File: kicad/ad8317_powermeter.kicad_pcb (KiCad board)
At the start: 2 copper layers, 18.2 x 13.5 mm, 37 parts, among them J1 Conn_Coaxial, U1 AD8317, U2 STM32F373RCTx, U3 REF3030, U4 ADP150AUJZ-3.3-R7

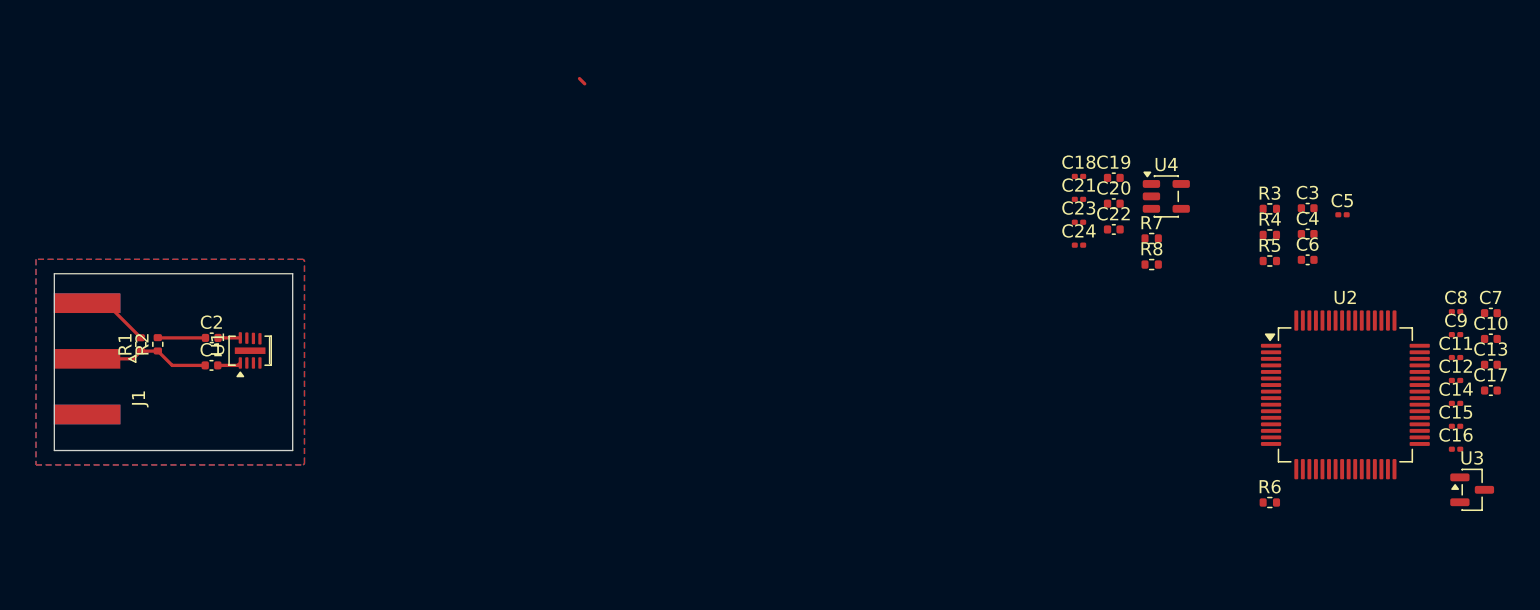
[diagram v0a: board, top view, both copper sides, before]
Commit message: Add calibration scripts, documentation, simulation tools, and KiCad updates
- cal/calibration.py: 3-phase RF linearity calibration (29 freq, 28 power steps,
  1 MHz–10 GHz, direct generator→DUT, no attenuator, NRP sensor 0.01 dBm precision)
- cal/temp_calibration.py: temperature calibration via Vötsch chamber (16–40°C,
  Vötsch SIMSERV TCP driver, tracking generator source, outputs TEMP_COEFF_DB_PER_C[])
- cal/results/: dry-run calibration tables (.h/.json), figures, PDF reports
- doc/: ADC signal path analysis, calibration procedure (3-phase), lab optimisation
  guide updated for 1 MHz–10 GHz range and temperature correction firmware formula
- doc/diagrams/: PlantUML/Mermaid source + rendered PNGs for pipeline, firmware,
  and RF signal chain architectures
- sim/ltpwr_to_touchstone.py: LTpowerAnalyzer Z(f) → Touchstone S1P + Z1P via
  scikit-rf for SIwave PI-AC Decoupling Optimization DC/DC source impedance import
- sim/Measured_source_impedance.txt/.s1p/.z1p: DC/DC output impedance measurement
  and converted Touchstone files (100 Hz–10 MHz, 201 points)
- kicad/: updated schematics (MCU, power management, RF frontend, UI) and PCB layout
- kicad/fixture-rev_A/: test fixture DXF drawings
- lib/: Würth 744231091 datasheet, Hammond 1590A board outline footprint
- pp_3d_printer_setup_spec.md, pp_horn_antenna_manufacturing_spec.md: process specs

Co-Authored-By: Claude Sonnet 4.6 <noreply@anthropic.com>
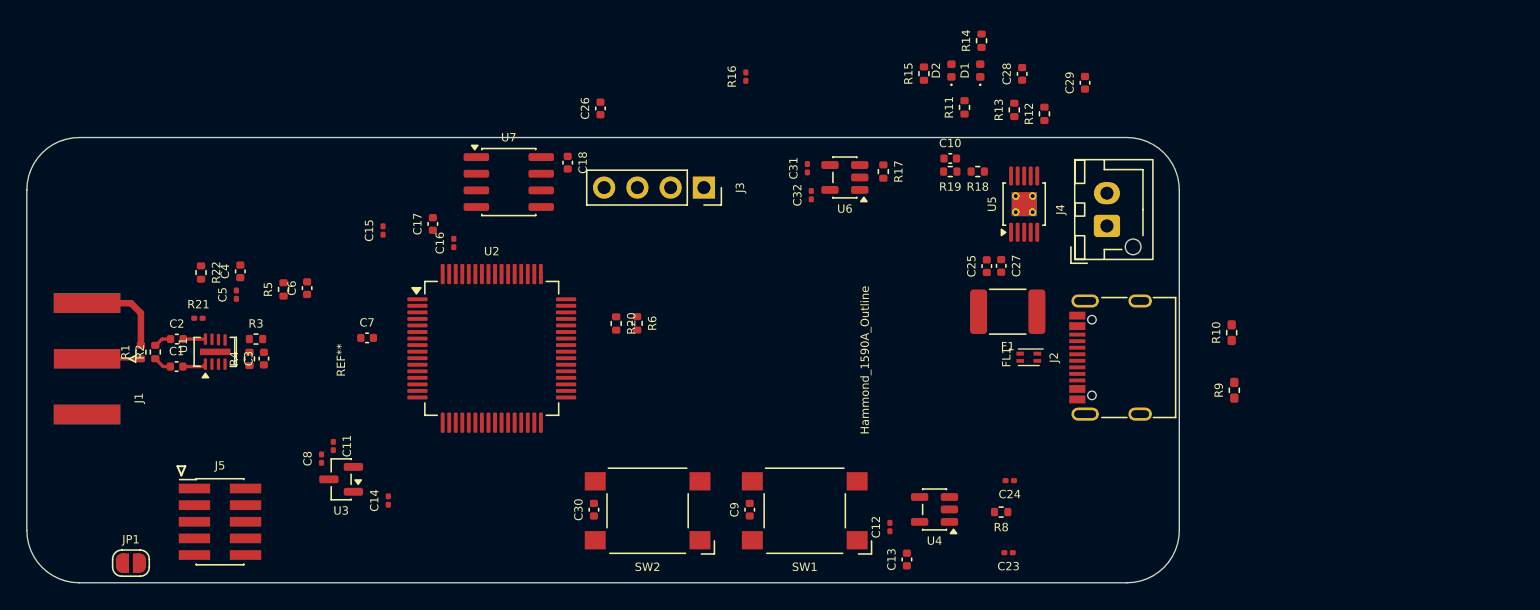
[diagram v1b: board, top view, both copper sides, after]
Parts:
- removed C19, C20: 100nF, Capacitor_SMD:C_0402_1005Metric
- removed C21: 10uF/, Capacitor_SMD:C_0201_0603Metric
- removed C22: 47nF, Capacitor_SMD:C_0402_1005Metric
- removed R7: 100R, Resistor_SMD:R_0402_1005Metric
- added C25: 100nF, Capacitor_SMD:C_0402_1005Metric, F.Cu at (206.4, 77.9)
- added C26: 100nF, Capacitor_SMD:C_0402_1005Metric, F.Cu at (176.9, 65.9)
- added C27: 100nF, Capacitor_SMD:C_0402_1005Metric, F.Cu at (207.5, 77.9)
- added C28: 10uF/16V, Capacitor_SMD:C_0402_1005Metric, F.Cu at (209.1, 63.2)
- added C29: 10uF/16V, Capacitor_SMD:C_0402_1005Metric, F.Cu at (213.9, 63.9)
- added C30: 100nF, Capacitor_SMD:C_0402_1005Metric, F.Cu at (176.4, 96.5)
- added C31: 1uF/, Capacitor_SMD:C_0201_0603Metric, F.Cu at (192.7, 70.4)
- added C32: 1uF/, Capacitor_SMD:C_0201_0603Metric, F.Cu at (193.0, 72.5)
- added D1: LED, LED_SMD:LED_0402_1005Metric, F.Cu at (205.9, 63.0)
- added D2: LED, LED_SMD:LED_0402_1005Metric, F.Cu at (203.7, 63.0)
- added F1: 2A max / 8V max, Fuse:Fuse_1812_4532Metric_Pad1.30x3.40mm_HandSolder, F.Cu at (208.0, 81.4)
- added FL1: 0603USB-142, Inductor_SMD:L_CommonModeChoke_Coilcraft_0603USB, F.Cu at (209.6, 84.9)
- added J2: USB_C_Receptacle_USB2.0_16P, Connector_USB:USB_C_Receptacle_G-Switch_GT-USB-7010ASV, F.Cu at (217.0, 84.9)
- added J3: Conn_01x04_Pin, Connector_PinSocket_2.54mm:PinSocket_1x04_P2.54mm_Vertical, F.Cu at (184.8, 71.9)
- added J4: Conn_01x02_Pin, Connector_JST:JST_XH_B2B-XH-AM_1x02_P2.50mm_Vertical, F.Cu at (215.6, 74.8)
- added J5: Conn_ARM_JTAG_SWD_10_UART, Connector_PinHeader_1.27mm:PinHeader_2x05_P1.27mm_Vertical_SMD, F.Cu at (147.8, 97.4)
- added JP1: Small_Open, Jumper:SolderJumper-2_P1.3mm_Open_RoundedPad1.0x1.5mm, F.Cu at (141.1, 100.6)
- added R10: 5K1, Resistor_SMD:R_0402_1005Metric_Pad0.72x0.64mm_HandSolder, F.Cu at (225.1, 83.0)
- added R11: 1k, Resistor_SMD:R_0402_1005Metric, F.Cu at (204.7, 65.8)
- added R12: 2k, Resistor_SMD:R_0402_1005Metric, F.Cu at (210.8, 66.3)
- added R13: 0R, Resistor_SMD:R_0402_1005Metric, F.Cu at (208.5, 66.0)
- added R14: 1k5, Resistor_SMD:R_0402_1005Metric, F.Cu at (206.0, 60.7)
- added R15: 1k5, Resistor_SMD:R_0402_1005Metric, F.Cu at (201.6, 63.2)
- added R16: 10k NTC Thermistor, Capacitor_SMD:C_0201_0603Metric, F.Cu at (188.0, 63.5)
- added R17: 100k, Resistor_SMD:R_0402_1005Metric, F.Cu at (198.5, 70.7)
- added R18: 100k, Resistor_SMD:R_0402_1005Metric, F.Cu at (205.7, 70.7)
- added R19: 100k, Resistor_SMD:R_0402_1005Metric, F.Cu at (203.6, 70.7)
- added R20: 10K, Resistor_SMD:R_0402_1005Metric, F.Cu at (178.1, 82.3)
- added R21: 10k NTC Thermistor, Capacitor_SMD:C_0201_0603Metric, F.Cu at (146.2, 81.9)
- added R22: 100k, Resistor_SMD:R_0402_1005Metric, F.Cu at (146.4, 78.4)
- added R9: 5K1, Resistor_SMD:R_0402_1005Metric_Pad0.72x0.64mm_HandSolder, F.Cu at (225.3, 87.4)
- added REF**: Hammond_1590A_Outline, ad8317_custom:Hammond_1590A_Board_Outline, F.Cu at (177.1, 85.1)
- added SW1: SW_Omron_B3FS, Button_Switch_SMD:SW_SPST_Omron_B3FS-100xP, F.Cu at (192.5, 96.6)
- added SW2: SW_Omron_B3FS, Button_Switch_SMD:SW_SPST_Omron_B3FS-100xP, F.Cu at (180.5, 96.6)
- added U5: BQ24092DGQ, Package_SO:HVSSOP-10-1EP_3x3mm_P0.5mm_EP1.83x1.89mm_ThermalVias, F.Cu at (209.3, 73.2)
- added U6: AP2112K-3.3, Package_TO_SOT_SMD:SOT-23-5, F.Cu at (195.6, 71.2)
- added U7: M24C02-WMN, Package_SO:SOIC-8_3.9x4.9mm_P1.27mm, F.Cu at (169.9, 71.5)
- C18: value 1uF/ -> 100nF; footprint Capacitor_SMD:C_0201_0603Metric -> Capacitor_SMD:C_0402_1005Metric
- C3: value 1nF -> 1nF / C0G
- C6: value 8.2pF -> 8.2pF / C0G
- C7: value 47nF -> 100nF
- C9: value 10uF/ -> 100nF; footprint Capacitor_SMD:C_0201_0603Metric -> Capacitor_SMD:C_0402_1005Metric
- R4: value 100R -> 1k
- R5: value 0R -> 12k
- R6: value 100R -> 10K
- moved C8 87.4 mm to (155.6, 92.6), turned to 90 degrees
- moved U3 86.4 mm to (157.1, 94.2), turned to 180 degrees
- moved C11 86.0 mm to (156.5, 91.7), turned to -90 degrees
- moved C7 85.8 mm to (159.1, 83.4)
- moved C5 84.7 mm to (149.1, 80.1), turned to 90 degrees
- moved C15 83.3 mm to (160.3, 75.2), turned to 90 degrees
- moved C14 81.9 mm to (160.7, 95.8), turned to 90 degrees
- moved C17 81.8 mm to (164.1, 74.7), turned to 90 degrees
- moved C4 81.6 mm to (149.4, 78.3), turned to 90 degrees
- moved C3 80.5 mm to (151.2, 85.0), turned to 90 degrees
- moved R4 78.5 mm to (150.1, 85.0), turned to 90 degrees
- moved C16 78.1 mm to (165.7, 76.2), turned to 90 degrees
- moved R3 78.0 mm to (150.6, 83.5)
- moved C6 76.4 mm to (154.5, 79.6), turned to 90 degrees
- moved R5 75.3 mm to (152.7, 79.7), turned to 90 degrees
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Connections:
- C10 pad 1: unconnected-(C10-Pad1) -> GND
- C10 pad 2: unconnected-(C10-Pad2) -> Net-(U2-PB1)
- C18 pad 1: GND -> /MCU/+3V3
- C18 pad 2: /MCU/+3V3 -> GND
- C23 pad 2: /MCU/+3V3 -> /MCU/VBAT
- C7 pad 1: unconnected-(C7-Pad1) -> GND
- C7 pad 2: unconnected-(C7-Pad2) -> /MCU/NRST
- C9 pad 1: unconnected-(C9-Pad1) -> GND
- C9 pad 2: unconnected-(C9-Pad2) -> Net-(U2-PC8)
- R6 pad 1: unconnected-(R6-Pad1) -> /MCU/+3V3
- R6 pad 2: unconnected-(R6-Pad2) -> /MCU/I2C_SCL
- U2 pad 1: unconnected-(U2-VBAT-Pad1) -> /MCU/+3V3
- U2 pad 18: unconnected-(U2-PA3-Pad18) -> /MCU/JTAG_TDO
- U2 pad 24: unconnected-(U2-PC4-Pad24) -> /MCU/UART_RX
- U2 pad 25: unconnected-(U2-PC5-Pad25) -> /MCU/UART_TX
- U2 pad 26: unconnected-(U2-PB0-Pad26) -> /MCU/VDET
- U2 pad 27: unconnected-(U2-PB1-Pad27) -> Net-(U2-PB1)
- U2 pad 28: unconnected-(U2-PB2-Pad28) -> Net-(U2-PB2)
- U2 pad 39: unconnected-(U2-PC8-Pad39) -> Net-(U2-PC8)
- U2 pad 40: unconnected-(U2-PC9-Pad40) -> Net-(U2-PC9)
- U2 pad 42: unconnected-(U2-PA9-Pad42) -> /MCU/I2C_SCL
- U2 pad 43: unconnected-(U2-PA10-Pad43) -> /MCU/I2C_SDA
- U2 pad 44: unconnected-(U2-PA11-Pad44) -> /MCU/USB_DM
- U2 pad 45: unconnected-(U2-PA12-Pad45) -> /MCU/USB_DP
- U2 pad 46: unconnected-(U2-PA13-Pad46) -> /MCU/JTAG_TMS
- U2 pad 49: unconnected-(U2-PA14-Pad49) -> /MCU/JTAG_TCK
- U2 pad 50: unconnected-(U2-PA15-Pad50) -> /MCU/JTAG_TDI
- U2 pad 7: unconnected-(U2-NRST-Pad7) -> /MCU/NRST
- U2 pad 9: unconnected-(U2-PC1-Pad9) -> /MCU/CHG_STAT
- U4 pad 1: /MCU/+3V3 -> /MCU/VBAT
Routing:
- net Net-(J1-In): track 9.72 -> 5.52 mm
- net GND: track 8.84 -> 9.74 mm
- net (no net): track 0.57 -> 0.00 mm
- removed copper zone on B.Cu, net GND
- removed copper zone on F.Cu, net GND
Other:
- board size 18.2 x 13.5 mm -> 88 x 34 mm
- copper layers 2 -> 4
- board text added: "0"
- board text added: "0 mm"
- board text added: "0,01 mm"
- board text added: "0,02"
- board text added: "0,035 mm"
- board text added: "0,1 mm"
- board text added: "1"
- board text added: "1,24 mm"
- board text added: "3,3"
- board text added: "4,4"
- board text added: "4,5"
- board text added: "B.Cu"
- board text added: "B.Mask"
- board text added: "B.Paste"
- board text added: "B.Silkscreen"
- board text added: "Bottom Silk Screen"
- board text added: "Bottom Solder Mask"
- board text added: "Bottom Solder Paste"
- board text added: "Color"
- board text added: "Dielectric 1"
- board text added: "Dielectric 2"
- board text added: "Dielectric 3"
- board text added: "Dry Film"
- board text added: "Epsilon R"
- board text added: "F.Cu"
- board text added: "F.Mask"
- board text added: "F.Paste"
- board text added: "F.Silkscreen"
- board text added: "FR4"
- board text added: "FR4 natural"
- board text added: "In1.Cu"
- board text added: "In2.Cu"
- board text added: "Layer Name"
- board text added: "Loss Tangent"
- board text added: "Material"
- board text added: "Not specified"
- board text added: "Thickness (mm)"
- board text added: "Top Silk Screen"
- board text added: "Top Solder Mask"
- board text added: "Top Solder Paste"
- board text added: "Type"
- board text added: "copper"
- board text added: "core"
- board text added: "prepreg"
